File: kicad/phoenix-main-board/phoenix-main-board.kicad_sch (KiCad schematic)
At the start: 87 parts, among them U1 LT3092xDD, U2 LM7705, U3 Adafruit_Feather_nrf52840_Exp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, U4 MCP3564, U5 TS5A3359, U6 TPS61222DCK, U7 OPA2380, U8 TPS7A2033DQN, U9 AD5242

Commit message: finish majority of pcb design
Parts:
- removed C10, C11: 100nF, Capacitor_SMD:C_0603_1608Metric, symbol Device:C_Small
- removed JP5: SolderJumper_2_Bridged, Jumper:SolderJumper-2_P1.3mm_Bridged_RoundedPad1.0x1.5mm, symbol Jumper:SolderJumper_2_Bridged
- removed JP6: SolderJumper_2_Open, Jumper:SolderJumper-2_P1.3mm_Open_RoundedPad1.0x1.5mm, symbol Jumper:SolderJumper_2_Open
- removed R13, R14: 100, Resistor_SMD:R_0603_1608Metric, symbol Device:R
- removed TP35: TestPoint_Small, TestPoint:TestPoint_Keystone_5000-5004_Miniature, symbol Connector:TestPoint_Small
- added JP1: SolderJumper_3_Bridged12, Jumper:SolderJumper-3_P1.3mm_Bridged2Bar12_Pad1.0x1.5mm, symbol Jumper:SolderJumper_3_Bridged12
- added R23, R24: 10k, Resistor_SMD:R_0603_1608Metric, symbol Device:R
- added TP27, TP37, TP5: TestPoint_Small, TestPoint:TestPoint_Keystone_5000-5004_Miniature, symbol Connector:TestPoint_Small
- D1, D2, PD1, PD2: footprint LED_THT:LED_D5.0mm -> LED_THT:LED_D5.0mm_Horizontal_O1.27mm_Z3.0mm
- TH2: footprint Connector_Wire:SolderWire-0.1sqmm_1x02_P3.6mm_D0.4mm_OD1mm_Relief -> Resistor_SMD:R_0603_1608Metric
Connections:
- net GNDA is gone; now on net GND: C12.2, C13.2, C4.2, C5.2, C6.2, U4.2 (AGND), U4.3 (REFIN-)
- net +3.3V: now also JP1.3 (B); no longer U7.5 (V+), U9.5 (VDD)
- net +3.3VA: now also U7.5 (V+), U9.5 (VDD), U9.6 (~{SHDN})
- net +5V: now also JP1.1 (A)
- net CH0: now also R23.2, R24.1
- net CH1: now also R21.2, TH2.1
- net CH2: now also R22.2, TH1.1, TP5.1; no longer C12.1, R15.1, TP3.1
- net CH3: no longer C13.1, R16.1, TP4.1
- net CH4: now also C12.1, R15.1, TP3.1
- net CH5: now also C13.1, R16.1, TP4.1
- net EnablePower: no longer U9.6 (~{SHDN})
- net GND: now also R24.2, TP27.1
- net IN1: no longer U3.25 (6_(D6))
- net IN2: no longer U3.26 (5_(D5))
- net MCLK: no longer U3.7 (16_(A2))
- net PD1_SIG: now also R15.2
- net PD2_SIG: now also R16.2
- net ~{IRQ}: now also TP37.1
- net at U1.7, U1.8: now also JP1.2 (C)
- removed net THERM1_SIG: R15.2, R21.2, TH2.1
- removed net THERM2_SIG: R16.2, R22.2, TH1.1
- net Thermistor1 renamed Thermistor_On
- net Thermistor_On: now also R22.1, R23.1
- net Thermistor2: no longer names the net of U3.23 (10_(D10))
- net Thermistor2: no longer R22.1
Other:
- moved on the sheet: C12, C13, R15, R16, R21, R22, TH1, TH2, TP25, TP26, TP3, TP4

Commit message: v1.0.0 release
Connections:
- net NO0: now reaches D1.1 (K), TP18.1, U5.1 (NO0)
- net NO1: now reaches D2.1 (K), TP19.1, U5.2 (NO1)
- net NO2: now reaches R3.1, TP20.1, U5.3 (NO2)
- net CSOURCE: now reaches D1.2 (A), D2.2 (A), R3.2, Rout1.1, Rset1.1, TP31.1
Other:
- note removed: "Goals for this iteration People can hand solder it if they need to. This could be like the "basic" version of the instrument, and I could follow it up with a "pro" model later"
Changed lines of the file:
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@@
 	(text "For this version, will use onboard battery charger of feather, and its simple\nbattery voltage monitor to account for charge. I can go fancier some other time if \nit seems actually necessary.\n\n\n"
 		(exclude_from_sim no)
-		(at 233.934 40.64 0)
+		(at 229.87 30.48 0)
 		(effects
 			(font
@@
 		)
 	)
-	(text "Goals for this iteration\nPeople can hand solder it if they need to. \nThis could be like the \"basic\" version of the instrument, and I could follow it up with a \"pro\" model later\n"
-		(exclude_from_sim no)
-		(at 226.822 21.336 0)
-		(effects
-			(font
-				(size 1.27 1.27)
-			)
-		)
-	)
 	(text "Photodiode Amplification"
 		(exclude_from_sim no)
@@
 	(text "thinking I'm just gonna use mcp3561 on this guy. 24 bit, $3, and high sample rate with low temp drift. \nI think it's our best best for starting out simple"
 		(exclude_from_sim no)
-		(at 225.806 32.512 0)
+		(at 225.552 19.05 0)
 		(effects
 			(font
@@
 		)
 	)
+	(label "NO1"
+		(at 50.8 246.38 0)
+		(effects
+			(font
+				(size 1.27 1.27)
+			)
+			(justify left bottom)
+		)
+	)
 	(label "CH2"
 		(at 330.2 95.25 180)
@@
 		)
 	)
+	(label "NO0"
+		(at 59.69 242.57 0)
+		(effects
+			(font
+				(size 1.27 1.27)
+			)
+			(justify left bottom)
+		)
+	)
 	(label "SDA"
 		(at 250.19 233.68 180)
@@
 		)
 	)
+	(label "NO2"
+		(at 49.53 250.19 0)
+		(effects
+			(font
+				(size 1.27 1.27)
+			)
+			(justify left bottom)
+		)
+	)
+	(label "CSOURCE"
+		(at 60.96 231.14 0)
+		(effects
+			(font
+				(size 1.27 1.27)
+			)
+			(justify left bottom)
+		)
+	)

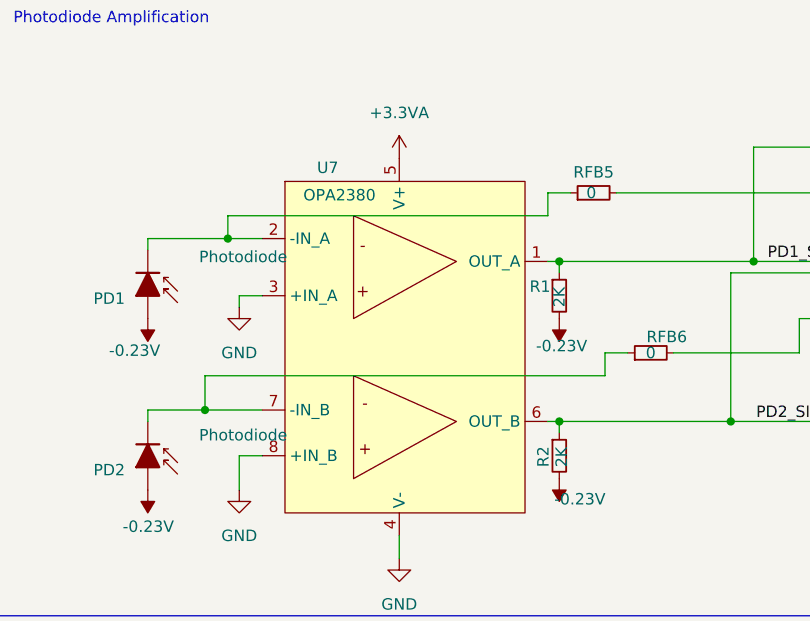
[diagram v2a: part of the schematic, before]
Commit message: PCB: Fix OPA2380 pinout
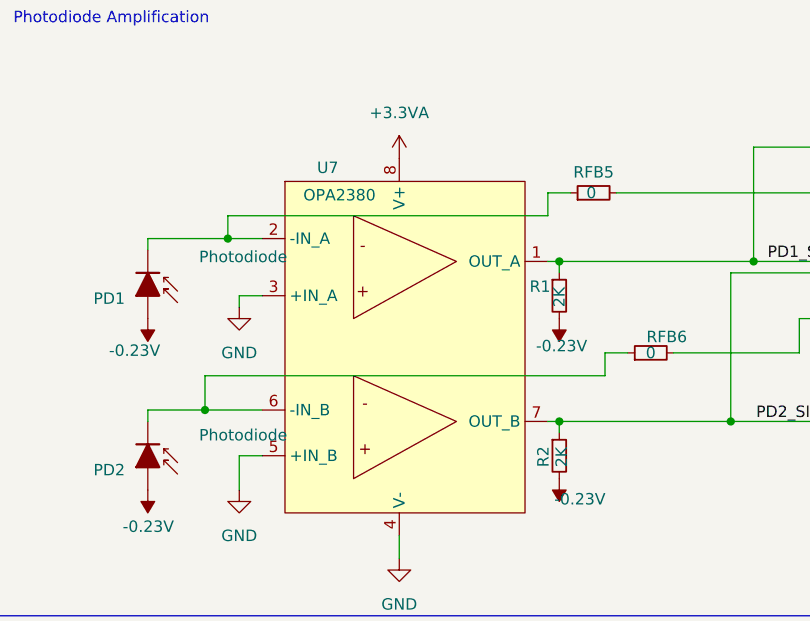
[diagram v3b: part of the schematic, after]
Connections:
- net +3.3VA: now also U7.8 (V+); no longer U7.5 (V+)
- net GND: now also U7.5 (+IN_B); no longer U7.8 (+IN_B)
- net PD2_SIG: now also U7.7 (OUT_B); no longer U7.6 (OUT_B)
- net at PD2.1 (K), RFB6.1: now also U7.6 (-IN_B); no longer U7.7 (-IN_B)

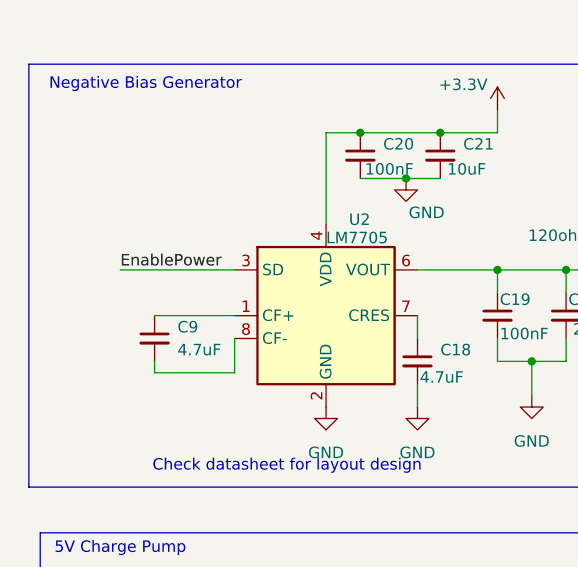
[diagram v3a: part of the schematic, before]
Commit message: PCB: Fix LM7705 SD wrong polarity
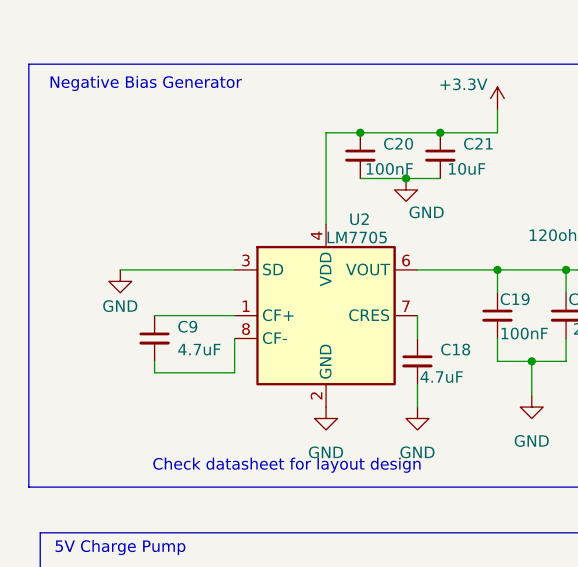
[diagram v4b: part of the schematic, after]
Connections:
- net EnablePower: no longer U2.3 (SD)
- net GND: now also U2.3 (SD)
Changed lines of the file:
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@@
 		)
 	)
-	(label "EnablePower"
-		(at 25.4 130.81 0)
-		(effects
-			(font
-				(size 1.27 1.27)
-			)
-			(justify left bottom)
-		)
-	)
 	(label "SCL"
 		(at 82.55 78.74 180)
@@
 					(unit 1)
 				)
+			)
+		)
+	)
+	(symbol
+		(lib_id "power:GND")
+		(at 25.4 130.81 0)
+		(unit 1)
+		(exclude_from_sim no)
+		(in_bom yes)
+		(on_board yes)
+		(dnp no)
+		(property "Reference" "#PWR05"
+			(at 25.4 137.16 0)
+			(effects
+				(font
+					(size 1.27 1.27)
+				)
+				(hide yes)
+			)
+		)
+		(property "Value" "GND"
+			(at 25.4 134.874 0)
+			(effects
+				(font
+					(size 1.27 1.27)
+				)
+			)
+		)
+		(property "Footprint" ""
+			(at 25.4 130.81 0)
+			(effects
+				(font
+					(size 1.27 1.27)
+				)
+				(hide yes)
+			)
+		)
+		(property "Datasheet" ""
+			(at 25.4 130.81 0)
+			(effects
+				(font
+					(size 1.27 1.27)
+				)
+				(hide yes)
+			)
+		)
+		(property "Description" "Power symbol creates a global label with name \"GND\" , ground"
+			(at 25.4 130.81 0)
+			(effects
+				(font
+					(size 1.27 1.27)
+				)
+				(hide yes)
+			)
+		)
+		(pin "1"
+		)
+		(instances
+			(project "phoenix-main-board"
+				(path "/8c64b4e9-9831-47d6-b522-c6dcea8b461a"
+					(reference "#PWR05")
+					(unit 1)
+				)

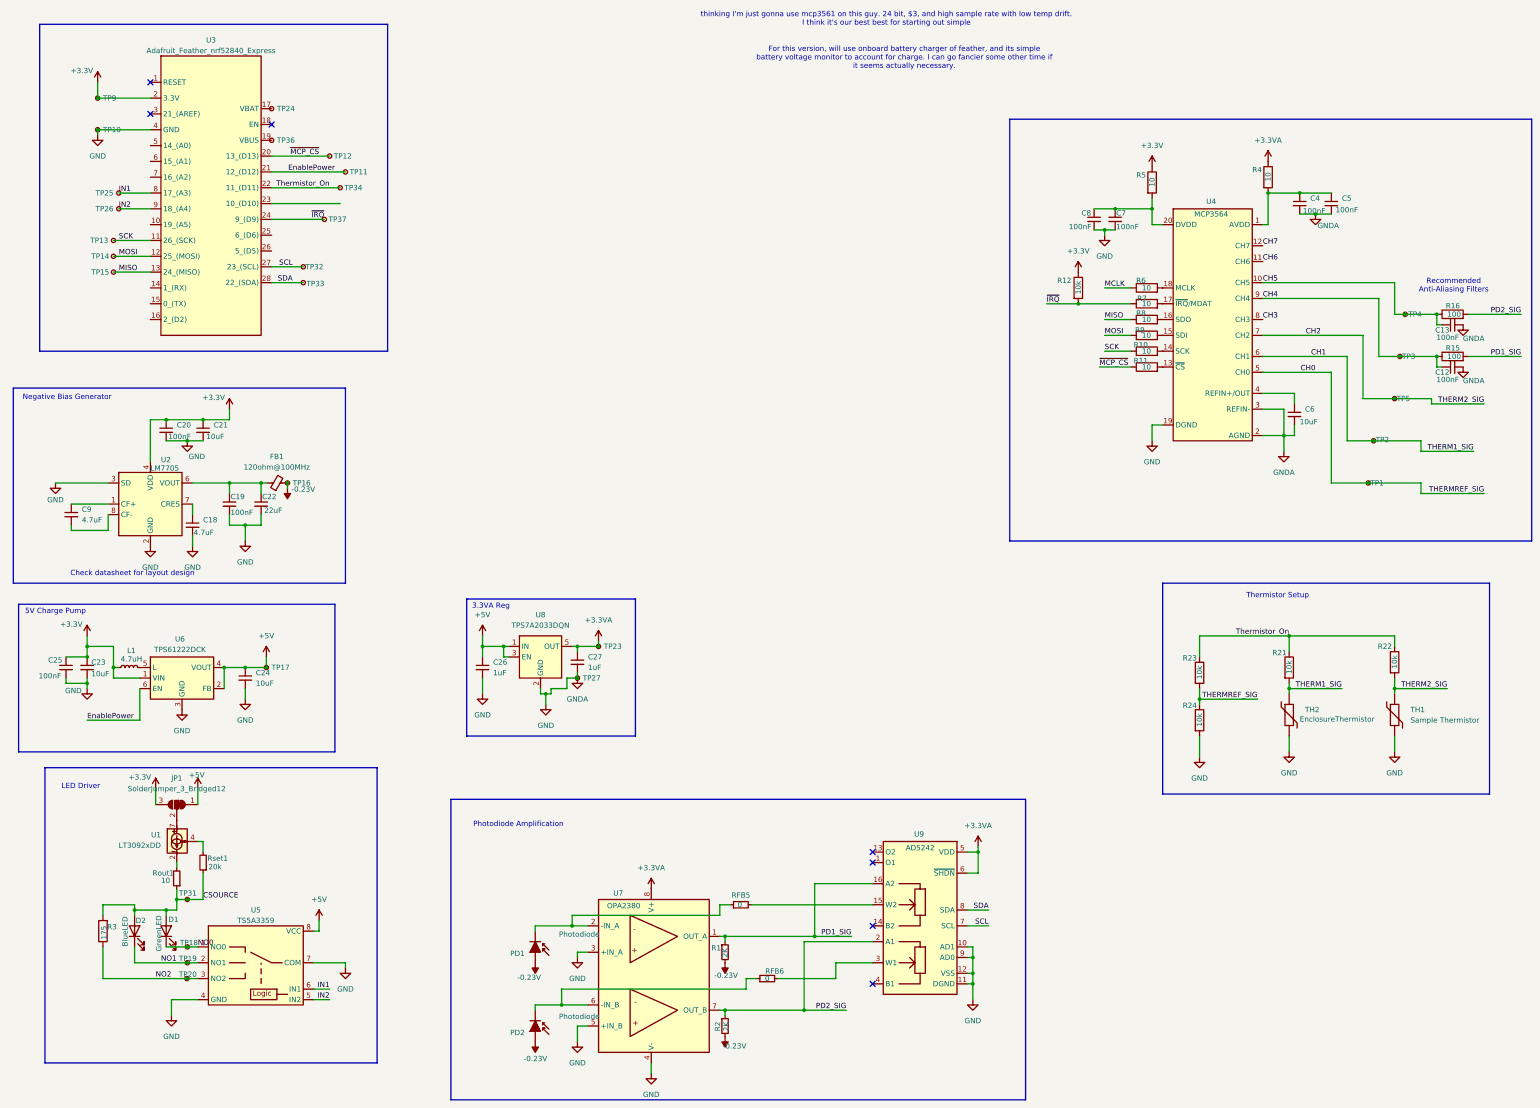
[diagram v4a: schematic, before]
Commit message: PCB: Update to V1.0.1. Begin preparation for production
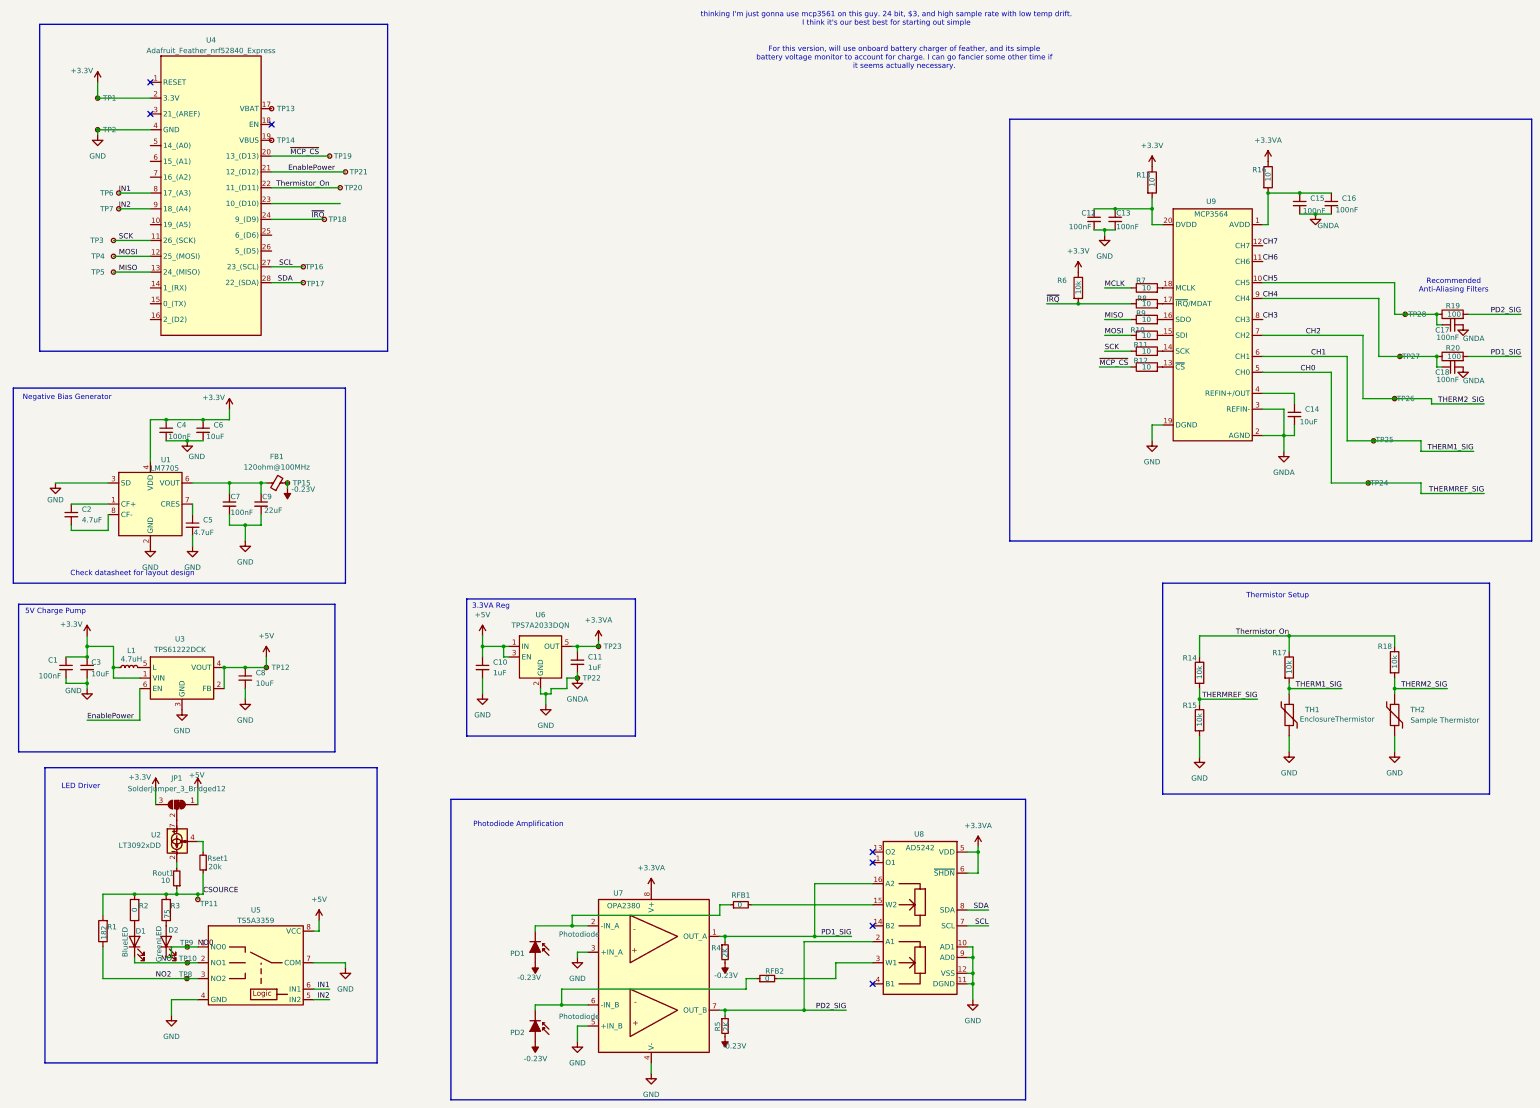
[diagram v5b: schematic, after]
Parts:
- added R2: 0, Resistor_SMD:R_0603_1608Metric, symbol Device:R
- added R3: 75, Resistor_SMD:R_0603_1608Metric, symbol Device:R
- PD1, PD2: footprint LED_THT:LED_D5.0mm_Horizontal_O1.27mm_Z3.0mm -> -ProjectLibrary:PD_Vertical
- R1: renamed from R3; value 175 -> 182
- renumbered C25 to C1, C26 to C10, C27 to C11, C8 to C12, C7 to C13, C6 to C14, C4 to C15, C5 to C16, C13 to C17, C12 to C18, C9 to C2, C23 to C3, C20 to C4, C18 to C5, C21 to C6, C19 to C7, C24 to C8, C22 to C9, D2 to D1, D1 to D2, R9 to R10, R10 to R11, R11 to R12, R5 to R13, R23 to R14, R24 to R15, R4 to R16, R21 to R17, R22 to R18, R16 to R19, R15 to R20, R1 to R4, R2 to R5, R12 to R6, R6 to R7, R7 to R8, R8 to R9, RFB5 to RFB1, RFB6 to RFB2, TH2 to TH1, TH1 to TH2, TP9 to TP1, TP19 to TP10, TP31 to TP11, TP17 to TP12, TP24 to TP13, TP36 to TP14, TP16 to TP15, TP32 to TP16, TP33 to TP17, TP37 to TP18, TP12 to TP19, TP10 to TP2, TP34 to TP20, TP11 to TP21, TP27 to TP22, TP1 to TP24, TP2 to TP25, TP5 to TP26, TP3 to TP27, TP4 to TP28, TP13 to TP3, TP14 to TP4, TP15 to TP5, TP25 to TP6, TP26 to TP7, TP20 to TP8, TP18 to TP9, U2 to U1, U1 to U2, U6 to U3, U3 to U4, U8 to U6, U9 to U8, U4 to U9
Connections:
- net CSOURCE: now also R2.2, R3.2; no longer D1.2 (A), D2.2 (A)
- new net: D1.2 (A), R2.1
- new net: D2.2 (A), R3.1
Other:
- moved on the sheet: D1, D2, TP11
